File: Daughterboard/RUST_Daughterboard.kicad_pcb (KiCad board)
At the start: 4 copper layers, 61.3 x 70 mm, 45 parts, among them J1 Conn_Coaxial, J2 SIM, J3 Conn_01x12, J6 Conn_01x12, J7 Micro_SD_Card_Det, K1 EE2-3TNU-L, U11 TXB0104D

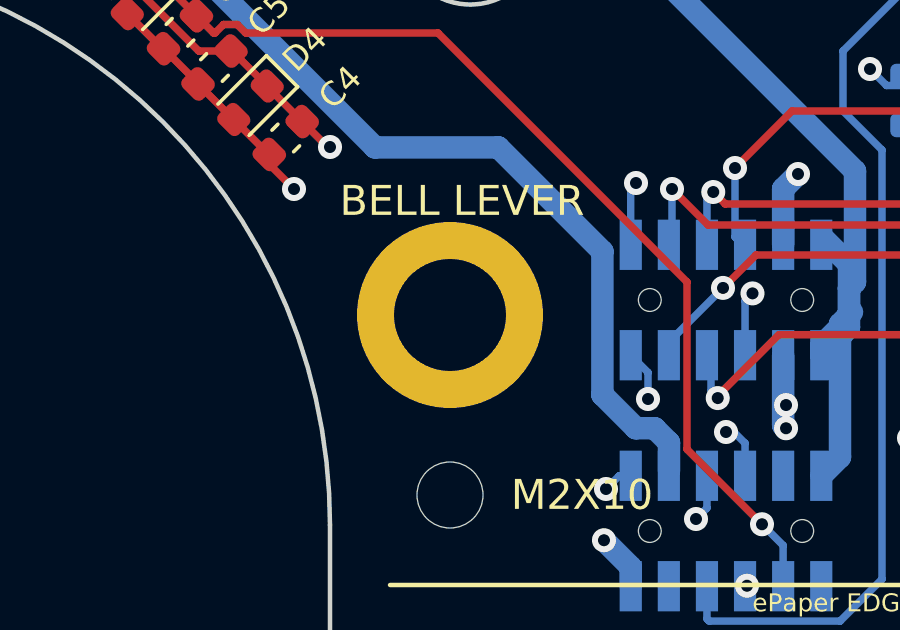
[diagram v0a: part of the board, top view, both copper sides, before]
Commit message: fixed part no.s for availability
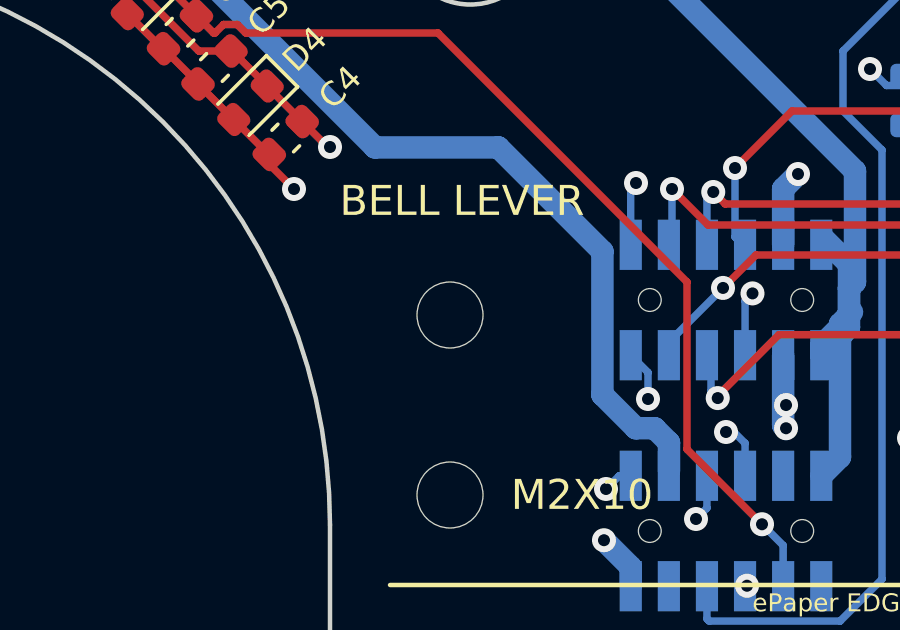
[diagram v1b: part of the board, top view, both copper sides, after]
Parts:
- MH3: value M2 SMT NUT -> MountingHole; footprint MyFootprints:SMTSO-M2-3ET -> MountingHole:MountingHole_2.2mm_M2

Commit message: for phase 1 prod
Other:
- board text added: "Fab notes: -BOARD THICKNESS: 1.6mm -Solder mask: black -Silk: White -Surface finish: ENIG"
- board text removed: "Fab notes: -Panel 2X2, 10mm RAIL -BOARD THICKNESS: 1.6mm -Solder mask: black -Silk: White -Surface finish: ENIG"
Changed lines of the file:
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@@
 		)
 	)
-	(gr_text "Fab notes:\n	-Panel 2X2, 10mm RAIL\n	-BOARD THICKNESS: 1.6mm\n	-Solder mask: black\n	-Silk: White\n	-Surface finish: ENIG"
+	(gr_text "Fab notes:\n	-BOARD THICKNESS: 1.6mm\n	-Solder mask: black\n	-Silk: White\n	-Surface finish: ENIG"
 		(at 73.35 48.8 0)
 		(layer "Cmts.User")
